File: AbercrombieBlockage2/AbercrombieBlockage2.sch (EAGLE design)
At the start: 35 parts, among them U1 DMN3135LVT, U2 ICS-43434, U3 CYBLE-022001-00, U4 LIS3DH, U5 VL53L0X, U6 VL53L0X, U7 VL53L0X, U8 M24

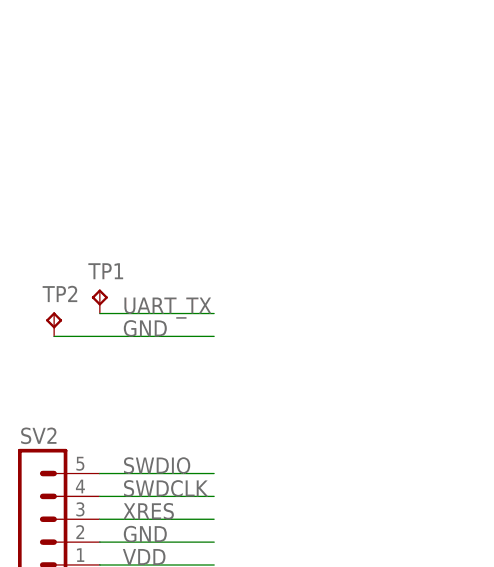
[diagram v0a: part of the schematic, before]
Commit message: Autorouted the AbercrombieLaser spray monitor
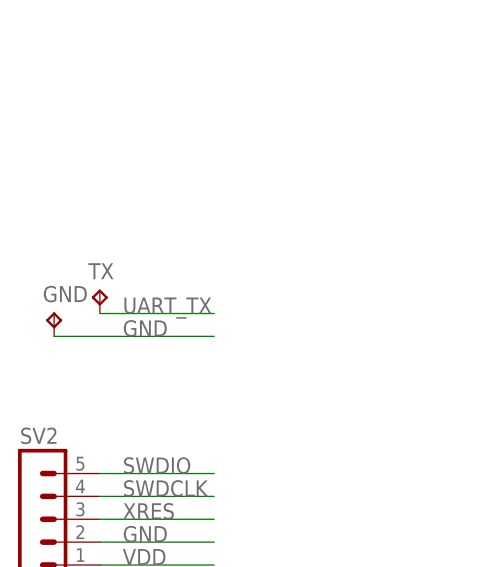
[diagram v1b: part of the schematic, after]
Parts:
- U2: DIGIKEY (none) -> 1428-1066-1-ND
- U3: DIGIKEY (none) -> 428-3566-PROMO-ND
- U4: DIGIKEY (none) -> 497-10613-1-ND
- U5, U6, U7: DIGIKEY (none) -> 497-16538-1-ND
- U8: DIGIKEY (none) -> 497-6348-1-ND
- renumbered TP1 to TX, TP2 to GND
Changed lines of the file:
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@@
 <part name="LED1" library="NicksParts" deviceset="LTST-C19HE1WT" device=""/>
 <part name="R2" library="resistor" deviceset="R-US_" device="R0603" value="360"/>
-<part name="U3" library="NicksParts" deviceset="CYBLE-022001-00" device=""/>
-<part name="U5" library="NicksParts" deviceset="VL53L0X" device=""/>
-<part name="U8" library="NicksParts" deviceset="M24" device=""/>
-<part name="U4" library="NicksParts" deviceset="LIS3DH" device=""/>
-<part name="U2" library="NicksParts" deviceset="ICS-43434" device=""/>
+<part name="U3" library="NicksParts" deviceset="CYBLE-022001-00" device="">
+<attribute name="DIGIKEY" value="428-3566-PROMO-ND"/>
+</part>
+<part name="U5" library="NicksParts" deviceset="VL53L0X" device="">
+<attribute name="DIGIKEY" value="497-16538-1-ND"/>
+</part>
+<part name="U8" library="NicksParts" deviceset="M24" device="">
+<attribute name="DIGIKEY" value="497-6348-1-ND"/>
+</part>
+<part name="U4" library="NicksParts" deviceset="LIS3DH" device="">
+<attribute name="DIGIKEY" value="497-10613-1-ND"/>
+</part>
+<part name="U2" library="NicksParts" deviceset="ICS-43434" device="">
+<attribute name="DIGIKEY" value="1428-1066-1-ND"/>
+</part>
 <part name="C6" library="resistor" deviceset="C-US" device="C0603" value="0.1u"/>
 <part name="GND5" library="supply1" deviceset="GND" device=""/>
@@
 <part name="C9" library="resistor" deviceset="C-US" device="C0603" value="4.7u"/>
 <part name="C13" library="resistor" deviceset="C-US" device="C0603" value="0.1u"/>
-<part name="U6" library="NicksParts" deviceset="VL53L0X" device=""/>
+<part name="U6" library="NicksParts" deviceset="VL53L0X" device="">
+<attribute name="DIGIKEY" value="497-16538-1-ND"/>
+</part>
 <part name="SUPPLY11" library="supply2" deviceset="V+" device=""/>
 <part name="GND11" library="supply1" deviceset="GND" device=""/>
 <part name="C10" library="resistor" deviceset="C-US" device="C0603" value="4.7u"/>
 <part name="C14" library="resistor" deviceset="C-US" device="C0603" value="0.1u"/>
-<part name="U7" library="NicksParts" deviceset="VL53L0X" device=""/>
+<part name="U7" library="NicksParts" deviceset="VL53L0X" device="">
+<attribute name="DIGIKEY" value="497-16538-1-ND"/>
+</part>
 <part name="SUPPLY12" library="supply2" deviceset="V+" device=""/>
 <part name="GND12" library="supply1" deviceset="GND" device=""/>
@@
 <part name="R5" library="resistor" deviceset="R-US_" device="R0603" value="360"/>
 <part name="BAT1" library="NicksParts" deviceset="SN2032" device=""/>
-<part name="TP1" library="testpad" deviceset="TP" device="B1,27"/>
-<part name="TP2" library="testpad" deviceset="TP" device="B1,27"/>
+<part name="TX" library="testpad" deviceset="TP" device="B1,27"/>
+<part name="GND" library="testpad" deviceset="TP" device="B1,27"/>
 <part name="R6" library="resistor" deviceset="R-US_" device="R0603" value="2M"/>
 <part name="R7" library="resistor" deviceset="R-US_" device="R0603" value="6.6M"/>
@@
 <instance part="LED1" gate="G$1" x="106.68" y="25.4"/>
 <instance part="R2" gate="G$1" x="111.76" y="10.16" rot="R270"/>
-<instance part="U3" gate="G$1" x="99.06" y="96.52"/>
-<instance part="U5" gate="G$1" x="200.66" y="109.22"/>
-<instance part="U8" gate="G$1" x="200.66" y="2.54"/>
-<instance part="U4" gate="G$1" x="200.66" y="149.86"/>
-<instance part="U2" gate="G$1" x="96.52" y="149.86"/>
+<instance part="U3" gate="G$1" x="99.06" y="96.52">
+<attribute name="DIGIKEY" x="99.06" y="96.52" size="1.778" layer="96" display="off"/>
+</instance>
+<instance part="U5" gate="G$1" x="200.66" y="109.22">
+<attribute name="DIGIKEY" x="200.66" y="109.22" size="1.778" layer="96" display="off"/>
+</instance>
+<instance part="U8" gate="G$1" x="200.66" y="2.54">
+<attribute name="DIGIKEY" x="200.66" y="2.54" size="1.778" layer="96" display="off"/>
+</instance>
+<instance part="U4" gate="G$1" x="200.66" y="149.86">
+<attribute name="DIGIKEY" x="200.66" y="149.86" size="1.778" layer="96" display="off"/>
+</instance>
+<instance part="U2" gate="G$1" x="96.52" y="149.86">
+<attribute name="DIGIKEY" x="96.52" y="149.86" size="1.778" layer="96" display="off"/>
+</instance>
 <instance part="C6" gate="G$1" x="134.62" y="152.4"/>
 <instance part="GND5" gate="1" x="99.06" y="66.04"/>
@@
 <instance part="C9" gate="G$1" x="236.22" y="109.22"/>
 <instance part="C13" gate="G$1" x="246.38" y="109.22"/>
-<instance part="U6" gate="G$1" x="200.66" y="71.12"/>
+<instance part="U6" gate="G$1" x="200.66" y="71.12">
+<attribute name="DIGIKEY" x="200.66" y="71.12" size="1.778" layer="96" display="off"/>
+</instance>
 <instance part="SUPPLY11" gate="1" x="231.14" y="83.82"/>
 <instance part="GND11" gate="1" x="231.14" y="53.34"/>
 <instance part="C10" gate="G$1" x="236.22" y="71.12"/>
 <instance part="C14" gate="G$1" x="246.38" y="71.12"/>
-<instance part="U7" gate="G$1" x="200.66" y="33.02"/>
+<instance part="U7" gate="G$1" x="200.66" y="33.02">
+<attribute name="DIGIKEY" x="200.66" y="33.02" size="1.778" layer="96" display="off"/>
+</instance>
 <instance part="SUPPLY12" gate="1" x="231.14" y="45.72"/>
 <instance part="GND12" gate="1" x="231.14" y="15.24"/>
@@
 <instance part="R5" gate="G$1" x="106.68" y="10.16" rot="R270"/>
 <instance part="BAT1" gate="1" x="0" y="63.5" rot="R90"/>
-<instance part="TP1" gate="G$1" x="-2.54" y="132.08"/>
-<instance part="TP2" gate="G$1" x="-7.62" y="129.54"/>
+<instance part="TX" gate="G$1" x="-2.54" y="132.08"/>
+<instance part="GND" gate="G$1" x="-7.62" y="129.54"/>
 <instance part="R6" gate="G$1" x="71.12" y="5.08" rot="R270"/>
 <instance part="R7" gate="G$1" x="71.12" y="20.32" rot="R270"/>
@@
 <wire x1="-7.62" y1="127" x2="10.16" y2="127" width="0.1524" layer="91"/>
 <label x="0" y="127" size="1.778" layer="95"/>
-<pinref part="TP2" gate="G$1" pin="TP"/>
+<pinref part="GND" gate="G$1" pin="TP"/>
 </segment>
 <segment>
@@
 <wire x1="-2.54" y1="129.54" x2="10.16" y2="129.54" width="0.1524" layer="91"/>
 <label x="0" y="129.54" size="1.778" layer="95"/>
-<pinref part="TP1" gate="G$1" pin="TP"/>
-</segment>
-<segment>
+<pinref part="TX" gate="G$1" pin="TP"/>
+</segment>
+<segment>
